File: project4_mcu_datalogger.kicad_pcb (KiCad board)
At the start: 2 copper layers, 49.6 x 30.5 mm, 30 parts, among them J1 Conn_01x09_Pin, J2 Conn_01x04_Pin, J3 Conn_01x04_Pin, J4 Conn_02x03_Odd_Even, U1 24LC1025, U2 DS1337S_T_R, U3 24LC1025, U4 ATMEGA328P-AU, Y1 32.768 KHz, Y2 16 MHz

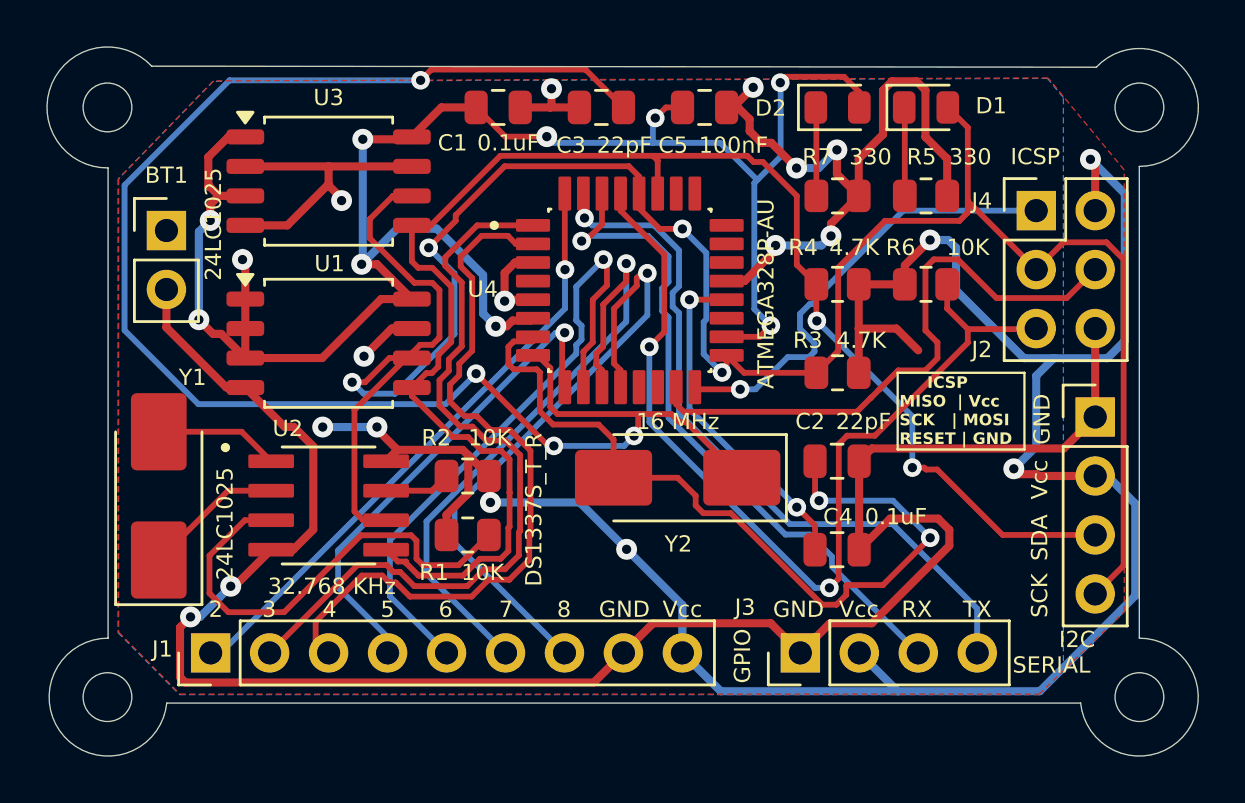
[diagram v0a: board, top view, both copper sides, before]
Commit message: Fixed bugs and completed 2-layer PCB
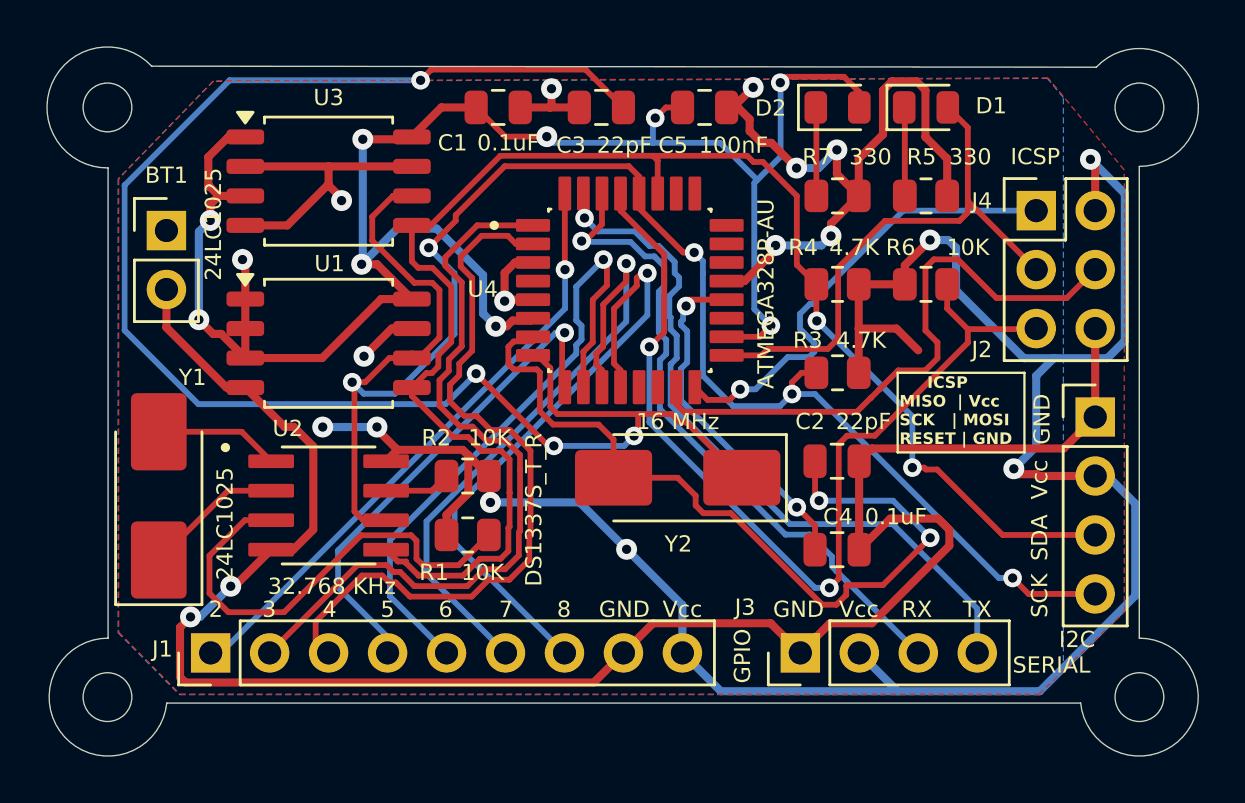
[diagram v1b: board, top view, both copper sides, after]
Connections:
- J2 pad 4: /SCK -> /SCL
- R3 pad 2: /SCK -> /SCL
- U1 pad 6: /SCK -> /SCL
- U2 pad 6: /SCK -> /SCL
- U3 pad 6: /SCK -> /SCL
- U4 pad 28: /SCK -> /SCL
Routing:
- net /SCK: track 99.3 -> 23.8 mm, vias 4 -> 0
- net /SCL: track 0.00 -> 74.5 mm, vias 0 -> 5
- net Net-(U4-AREF): track 14.8 -> 15.4 mm
